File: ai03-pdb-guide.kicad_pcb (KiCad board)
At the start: 2 copper layers, 81 x 38.1 mm, 24 parts, among them SW1 SW_Push, U1 ATmega32U4-AU, Y1 16MHz

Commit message: finished routing - I think
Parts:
- moved C4 3.13 mm to (107.4, -89.6), turned to 0 degrees
- moved R3 1.21 mm to (103.6, -86.7)
- moved C1 1.15 mm to (120.0, -70.9)
- moved C5 1.08 mm to (124.1, -86.0), turned to 180 degrees
- moved R4 0.73 mm to (125.0, -75.2)
- moved C6 0.19 mm to (105.7, -81.2), turned to 180 degrees
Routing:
- net GND: track 23.3 -> 131.5 mm
- net +5V: track 18.2 -> 108.7 mm, vias 0 -> 7
- net Net-(C3-Pad1): track 0.00 -> 16.0 mm
- net Net-(C2-Pad1): track 0.00 -> 11.7 mm
- net Net-(R3-Pad2): track 18.0 -> 29.2 mm
- net Net-(R4-Pad2): track 0.00 -> 4.21 mm
- net Net-(C6-Pad1): track 0.00 -> 3.15 mm

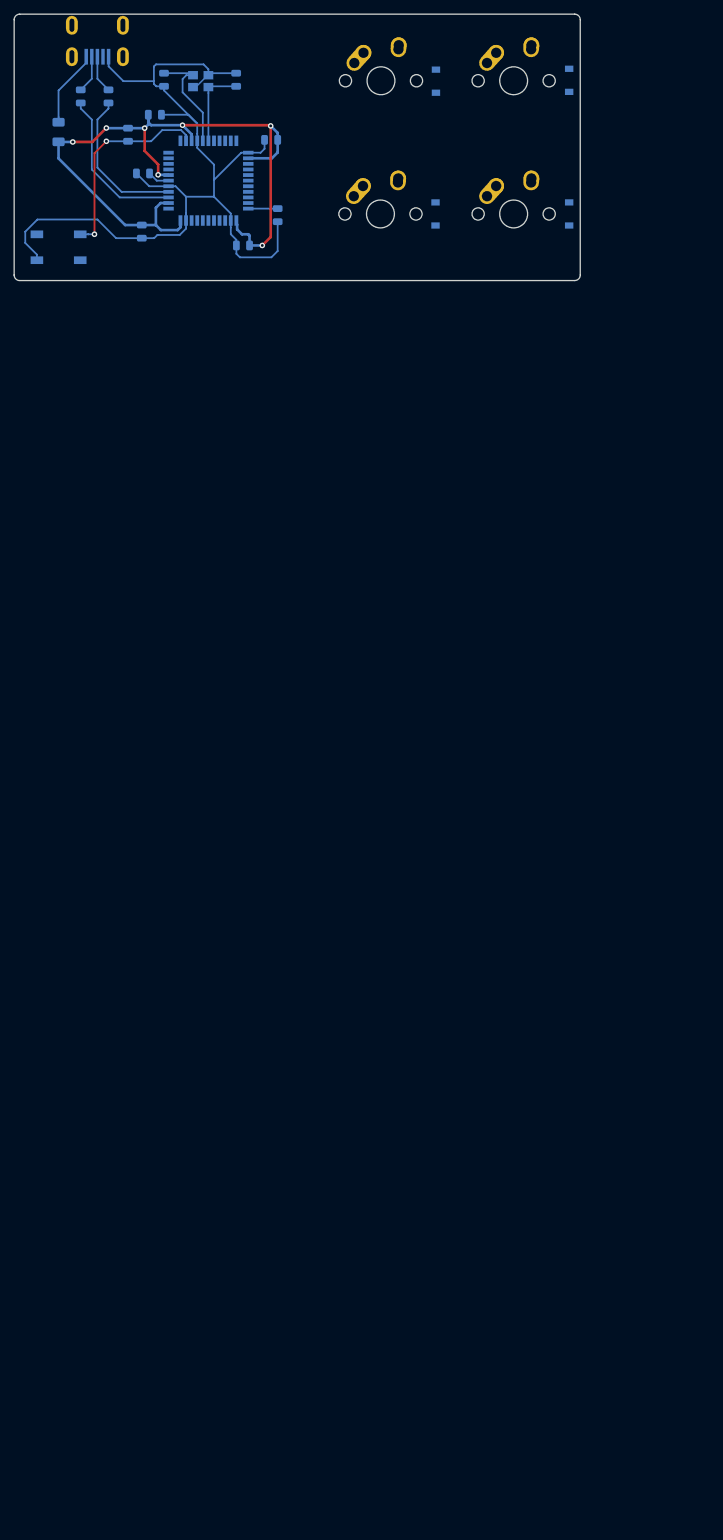
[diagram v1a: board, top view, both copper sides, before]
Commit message: fixed trace for power
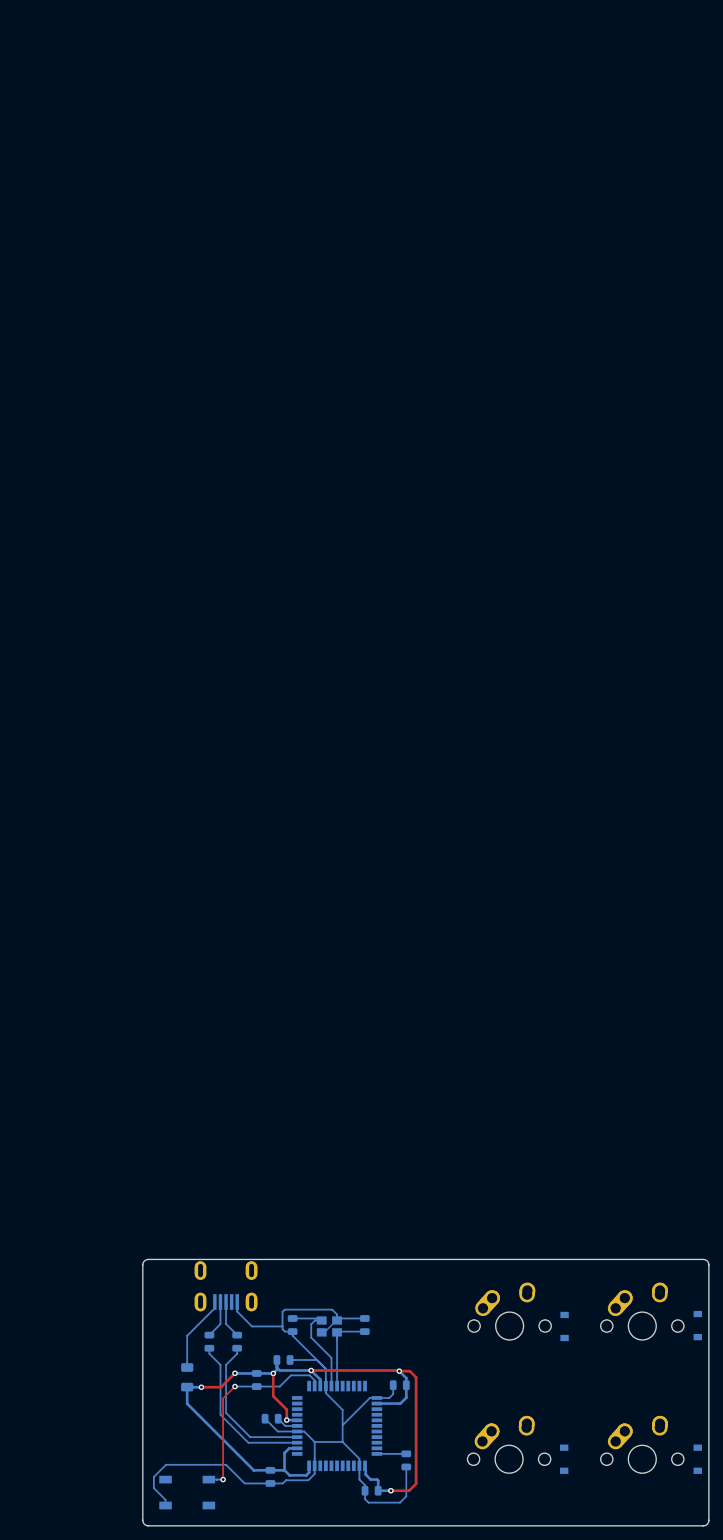
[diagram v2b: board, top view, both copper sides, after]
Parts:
- moved C1 179.0 mm to (138.4, 107.2)
- moved C6 179.0 mm to (124.1, 96.9)
- moved U1 179.0 mm to (133.5, 97.9)
- moved Y1 179.0 mm to (132.4, 83.7)
- moved C2 179.0 mm to (137.5, 83.5)
- moved C3 179.0 mm to (127.1, 83.5)
- moved C4 179.0 mm to (125.8, 88.5)
- moved C5 179.0 mm to (142.5, 92.1)
- moved C7 179.0 mm to (124.0, 105.2)
- moved D1 179.0 mm to (166.0, 83.7)
- moved D2 179.0 mm to (166.0, 102.7)
- moved D3 179.0 mm to (185.1, 83.6)
- moved D4 179.0 mm to (185.1, 102.7)
- moved F1 179.0 mm to (112.1, 91.0)
- moved MX1 179.0 mm to (158.2, 83.6)
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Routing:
- net +5V: track 108.7 -> 113.1 mm

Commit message: maybe finished routing
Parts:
- moved C4 1.34 mm to (125.0, 87.4), turned to 180 degrees
- moved R3 1.26 mm to (123.2, 91.1)
- moved C6 1.04 mm to (123.4, 96.2), turned to 90 degrees
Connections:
- U1 pad 27: Net-(U1-Pad27) -> ROW0
- U1 pad 28: Net-(U1-Pad28) -> COL1
- U1 pad 29: Net-(U1-Pad29) -> COL0
- U1 pad 30: Net-(U1-Pad30) -> ROW1
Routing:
- net COL1: track 0.00 -> 56.9 mm
- net ROW0: track 0.00 -> 52.9 mm
- net ROW1: track 0.00 -> 51.9 mm
- net COL0: track 0.00 -> 34.7 mm
- net GND: track 131.5 -> 144.1 mm
- net Net-(D4-Pad2): track 0.00 -> 6.62 mm
- net Net-(D3-Pad2): track 0.00 -> 6.59 mm
- net Net-(D1-Pad2): track 0.00 -> 6.57 mm
- net Net-(D2-Pad2): track 0.00 -> 6.56 mm
- net +5V: track 113.1 -> 106.7 mm, vias 7 -> 5
- net Net-(C6-Pad1): track 3.15 -> 4.74 mm
- net Net-(R3-Pad2): track 29.2 -> 28.4 mm
